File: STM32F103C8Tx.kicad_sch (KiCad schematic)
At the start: 16 parts, among them J1 ST-LINK, J2 UART_BOOT, J7 ST-LINKV2, J8 UART_BOOT, SW1 SW_Push, U1 STM32F103C8Tx, Y1 8MHz

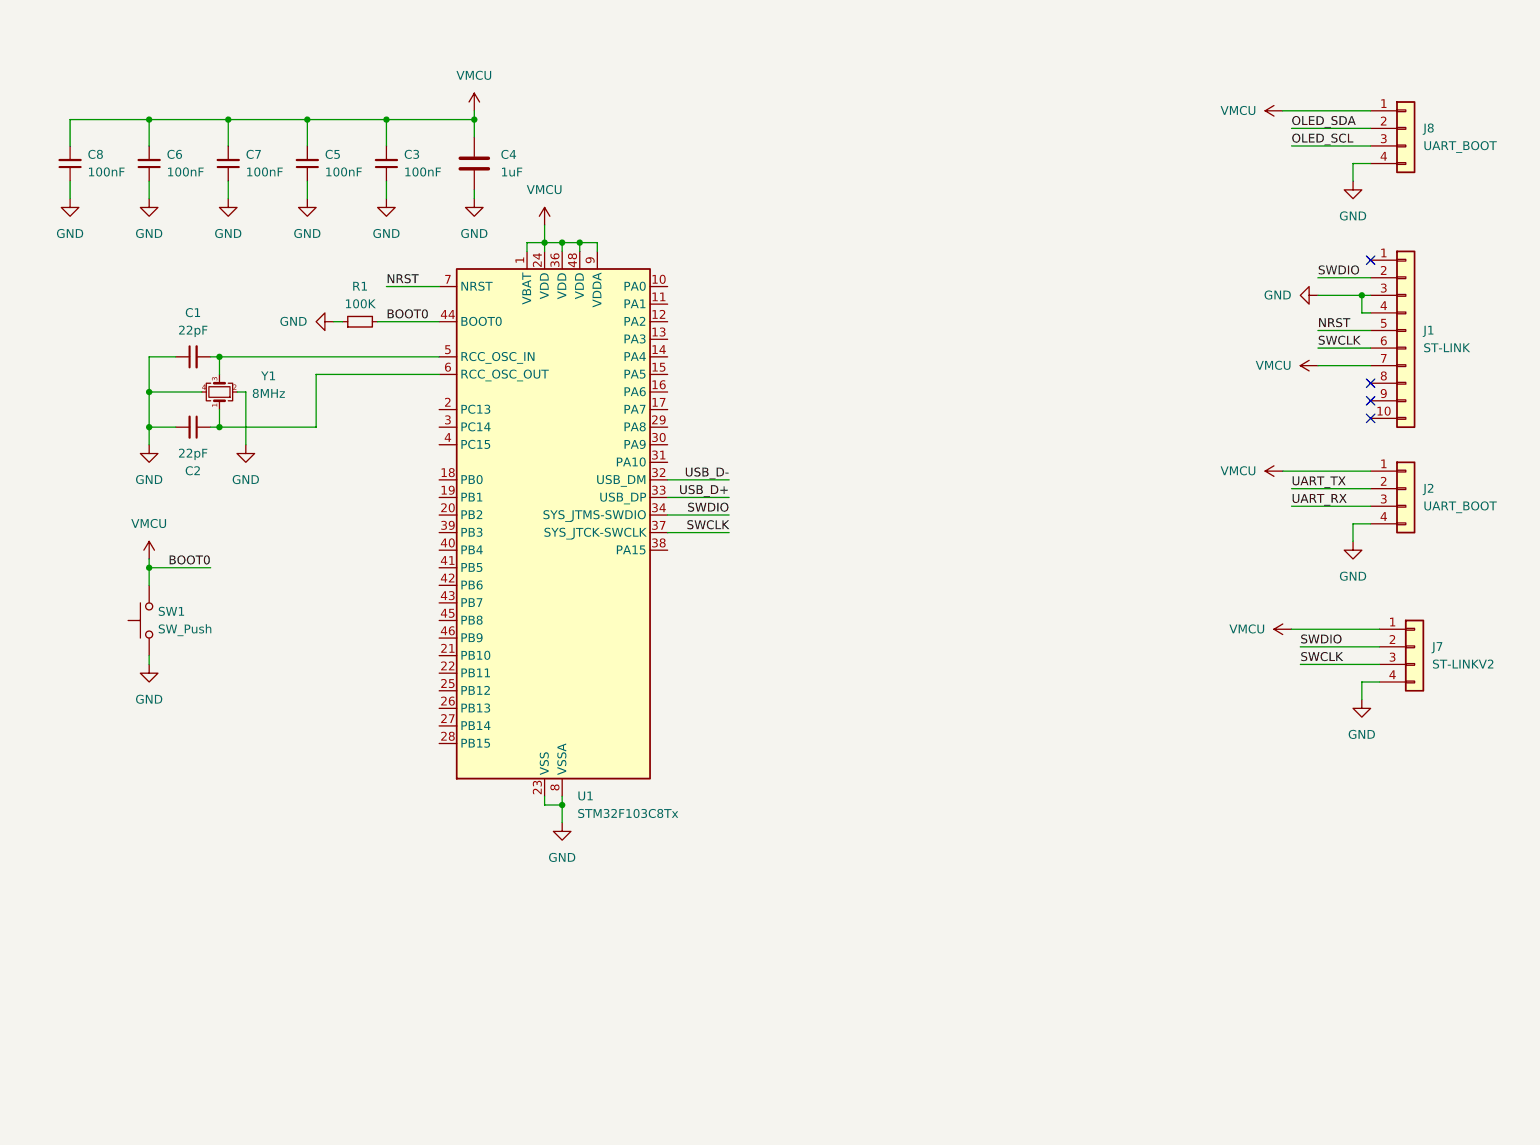
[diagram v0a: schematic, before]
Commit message: Added footwitch, usb led activity
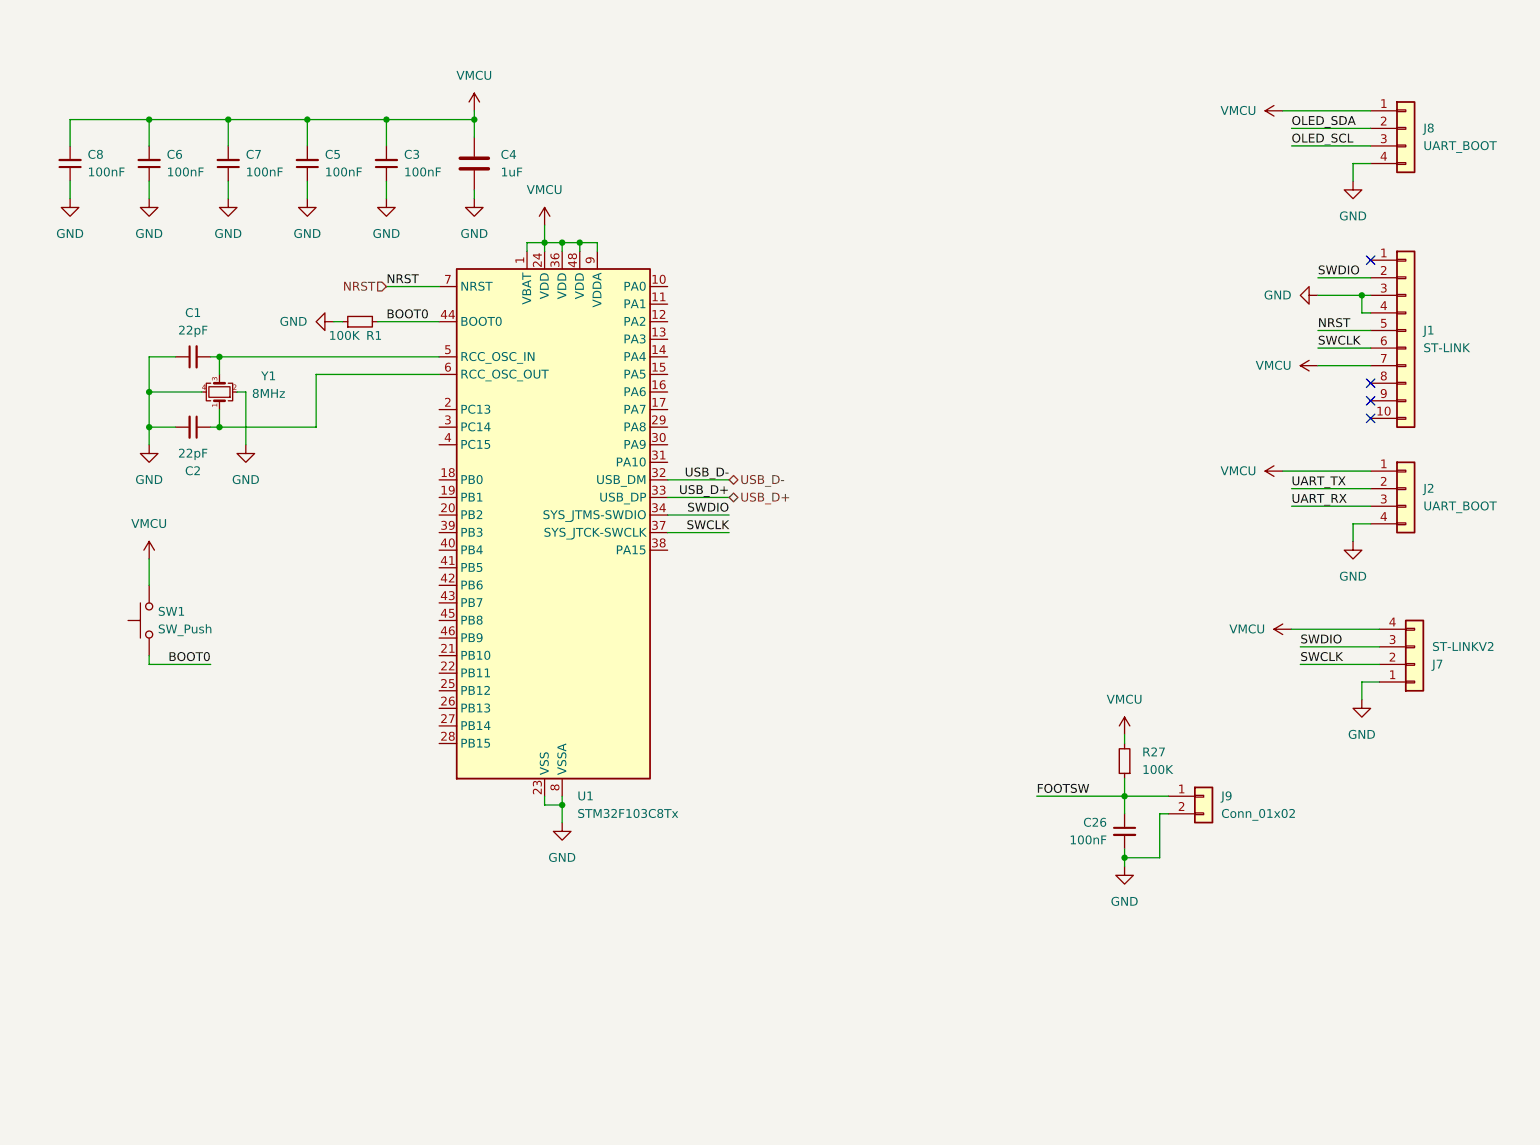
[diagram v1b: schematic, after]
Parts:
- added C26: 100nF, Capacitor_SMD:C_0603_1608Metric, symbol Device:C_Small
- added J9: Conn_01x02, Connector_JST:JST_PH_B2B-PH-K_1x02_P2.00mm_Vertical, symbol Connector_Generic:Conn_01x02
- added R27: 100K, Resistor_SMD:R_0603_1608Metric, symbol Device:R_Small
- C4: footprint Capacitor_SMD:C_0603_1608Metric -> Capacitor_SMD:C_0805_2012Metric
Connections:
- net GND: now also J7.1 (Pin_1), C26.2, J9.2 (Pin_2); no longer J7.4 (Pin_4), SW1.1
- net SWCLK: now also J7.2 (Pin_2); no longer J7.3 (Pin_3)
- net SWDIO: now also J7.3 (Pin_3); no longer J7.2 (Pin_2)
- net VMCU: now also J7.4 (Pin_4), R27.2; no longer J7.1 (Pin_1), R1.2, U1.44 (BOOT0)
- new net BOOT0: R1.2, SW1.1, U1.44 (BOOT0)
- new net FOOTSW: C26.1, J9.1 (Pin_1), R27.1

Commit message: layouting Power, Motor section
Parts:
- added R32, R33: 2.2K, Resistor_SMD:R_0603_1608Metric, symbol Device:R_Small
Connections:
- net OLED_SCL: now also R33.1
- net OLED_SDA: now also R32.1
- net VMCU: now also R32.2, R33.2

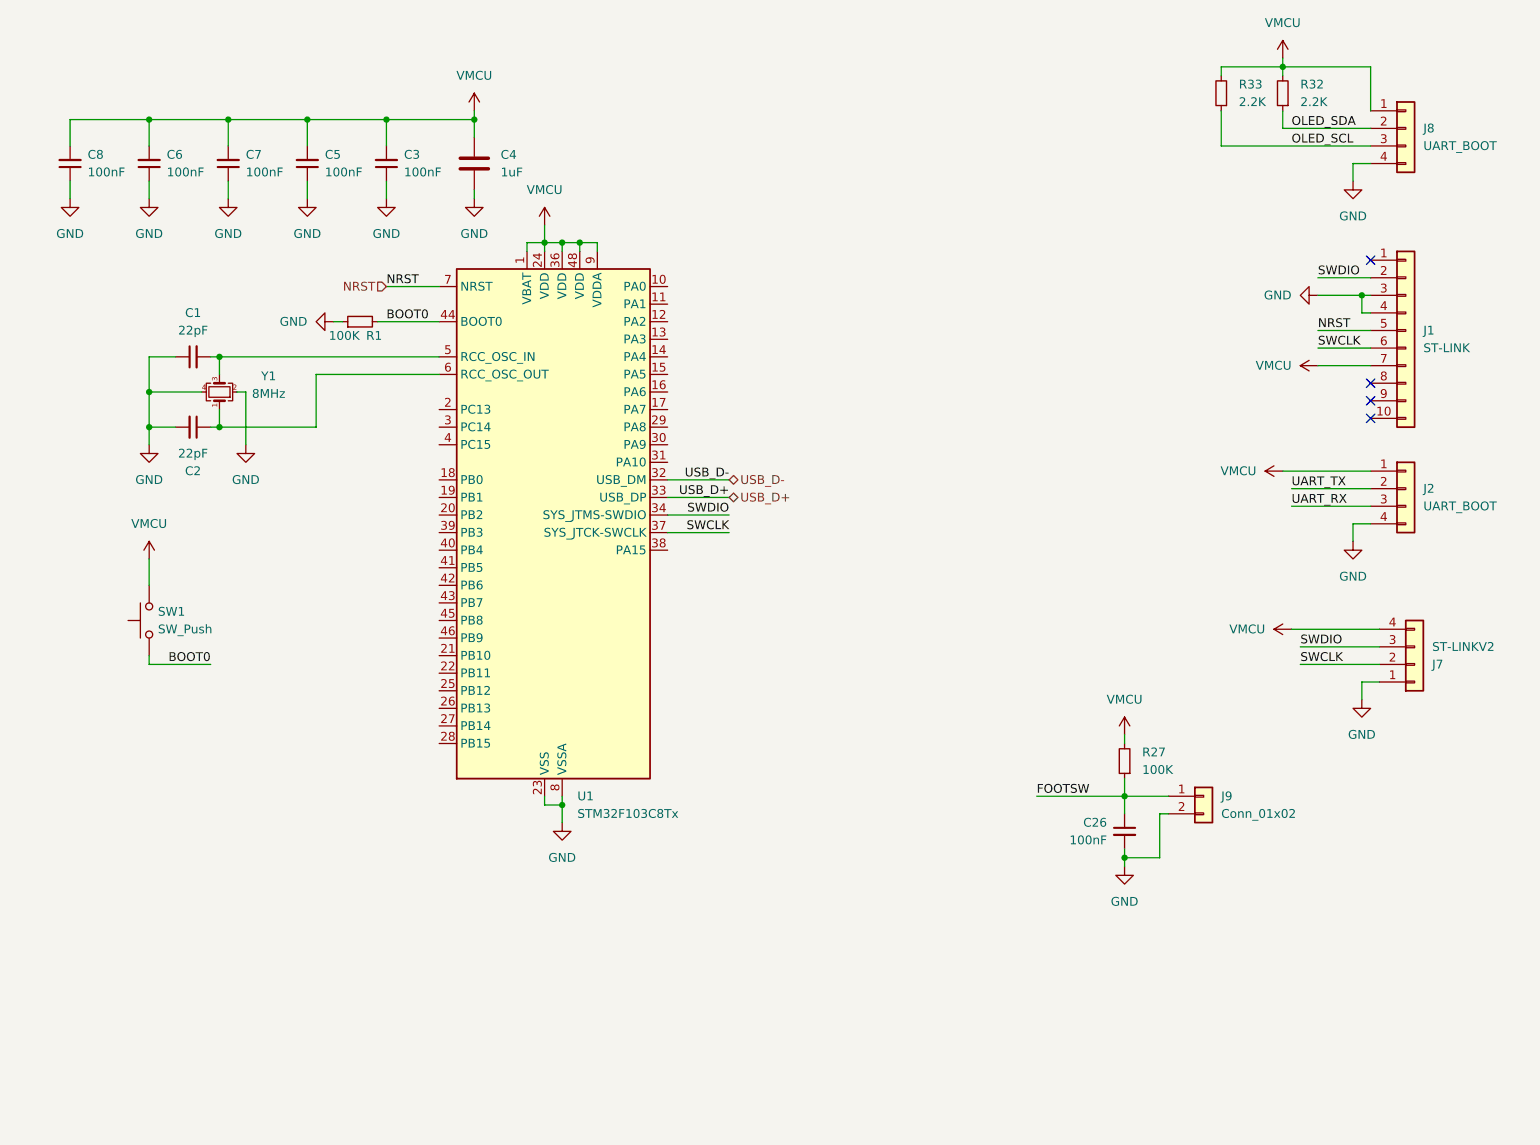
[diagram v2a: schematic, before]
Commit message: Added push button connector
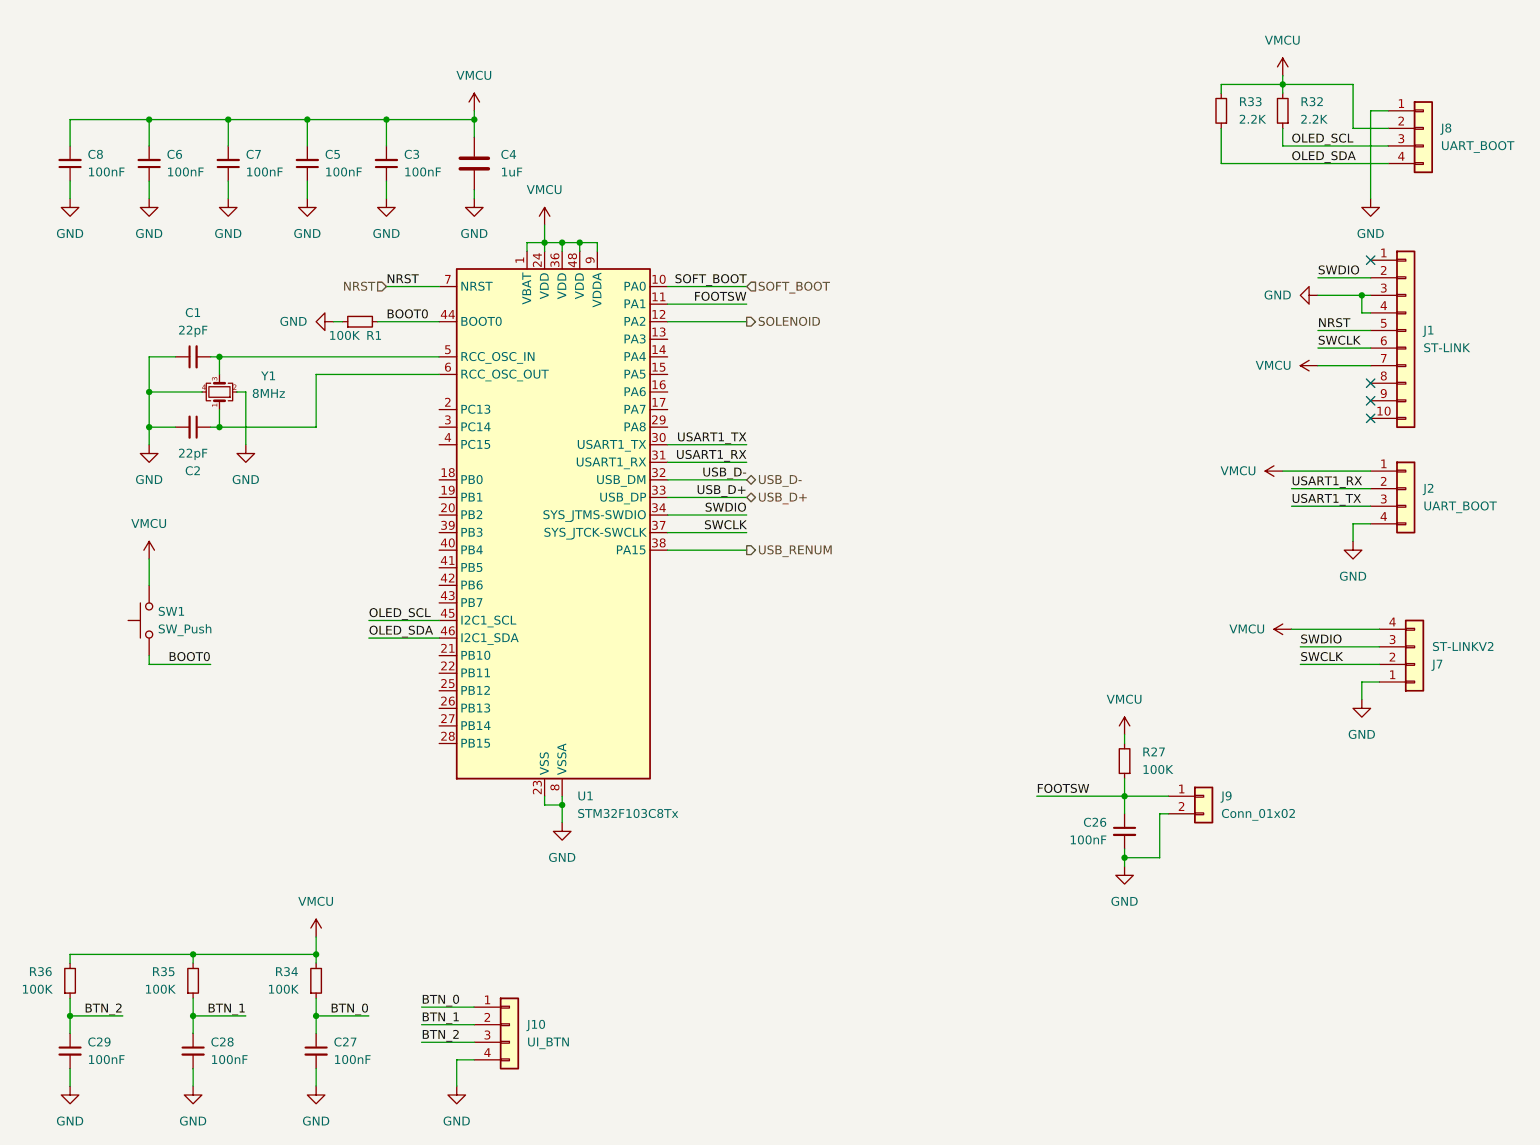
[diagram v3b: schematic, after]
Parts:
- added C27, C28, C29: 100nF, Capacitor_SMD:C_0603_1608Metric, symbol Device:C_Small
- added J10: UI_BTN, Connector_JST:JST_PH_B4B-PH-K_1x04_P2.00mm_Vertical, symbol Connector_Generic:Conn_01x04
- added R34, R35, R36: 100K, Resistor_SMD:R_0603_1608Metric, symbol Device:R_Small
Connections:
- net UART_RX is gone; now on net USART1_TX: J2.3 (Pin_3)
- net UART_TX is gone; now on net USART1_RX: J2.2 (Pin_2)
- net FOOTSW: now also U1.11 (PA1)
- net GND: now also J8.1 (Pin_1), C27.2, C28.2, C29.2, J10.4 (Pin_4); no longer J8.4 (Pin_4)
- net OLED_SCL: now also R32.1, U1.45 (PB8); no longer R33.1
- net OLED_SDA: now also J8.4 (Pin_4), R33.1, U1.46 (PB9); no longer J8.2 (Pin_2), R32.1
- net VMCU: now also J8.2 (Pin_2), R34.2, R35.2, R36.2; no longer J8.1 (Pin_1)
- net SOFT_BOOT: now reaches U1.10 (PA0)
- net SOLENOID: now reaches U1.12 (PA2)
- net USART1_TX: now reaches U1.30 (PA9)
- net USART1_RX: now reaches U1.31 (PA10)
- net USB_RENUM: now reaches U1.38 (PA15)
- new net BTN_0: C27.1, J10.1 (Pin_1), R34.1
- new net BTN_1: C28.1, J10.2 (Pin_2), R35.1
- new net BTN_2: C29.1, J10.3 (Pin_3), R36.1
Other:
- moved on the sheet: J8, R32, R33
